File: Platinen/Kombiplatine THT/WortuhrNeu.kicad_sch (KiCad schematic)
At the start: 101 parts, among them J1 Conn_01x01_Pin, J2 PROG MODE, J3 UART FLOATING, J4 UART, J5 Eingangsbuchse, SW1 PTS645Vx83-2LFS, SW2 PTS645Vx83-2LFS, U2 MCP1826-ADJE/ET, U3 Bluepill, U4 DS18B20, U6 Arduino_Nano_Every, U7 ESP-07, U8 Generic DCDC, U9 TP582, X1 Conn_01x03_Pin, X10 Conn_01x03_Pin, X11 Conn_01x03_Pin, X12 Conn_01x03_Pin, X13 Conn_01x03_Pin, X14 Conn_01x03_Pin, X15 Conn_01x03_Pin, X16 Conn_01x03_Pin, X17 Conn_01x03_Pin, X18 Conn_01x03_Pin, X19 Conn_01x03_Pin, X2 Conn_01x03_Pin, X20 Conn_01x03_Pin, X21 Conn_01x03_Pin, X22 Conn_01x03_Pin, X23 Conn_01x03_Pin, X24 Conn_01x03_Pin, X25 Conn_01x03_Pin, X26 Conn_01x03_Pin, X27 Conn_01x03_Pin, X28 Conn_01x03_Pin, X29 Conn_01x03_Pin, X3 Conn_01x03_Pin, X30 Conn_01x03_Pin, X31 Conn_01x03_Pin, X32 Conn_01x03_Pin, X33 Conn_01x03_Pin, X34 Conn_01x03_Pin, X35 Conn_01x03_Pin, X36 Conn_01x03_Pin, X37 Conn_01x03_Pin, X38 Conn_01x03_Pin, X4 Conn_01x03_Pin, X5 Conn_01x03_Pin, X6 Conn_01x03_Pin, X7 Conn_01x03_Pin, X8 Conn_01x03_Pin, X9 Conn_01x03_Pin

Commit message: Changes to Kombiplatine THT
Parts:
- J1: footprint TestPoint:TestPoint_Pad_1.0x1.0mm -> Connector_PinHeader_2.54mm:PinHeader_1x01_P2.54mm_Vertical
- U5: value ~ -> (none)
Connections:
- net +5V: now also X10.3 (Pin_3), X11.3 (Pin_3), X12.3 (Pin_3), X13.1 (Pin_1), X14.3 (Pin_3), X15.1 (Pin_1), X16.1 (Pin_1), X17.1 (Pin_1), X18.3 (Pin_3), X6.1 (Pin_1), X7.3 (Pin_3), X8.1 (Pin_1), X9.1 (Pin_1); no longer X10.1 (Pin_1), X11.1 (Pin_1), X12.1 (Pin_1), X13.3 (Pin_3), X14.1 (Pin_1), X15.3 (Pin_3), X16.3 (Pin_3), X17.3 (Pin_3), X18.1 (Pin_1), X6.3 (Pin_3), X7.1 (Pin_1), X8.3 (Pin_3), X9.3 (Pin_3)
- net GND: now also X10.1 (Pin_1), X11.1 (Pin_1), X12.1 (Pin_1), X13.3 (Pin_3), X14.1 (Pin_1), X15.3 (Pin_3), X16.3 (Pin_3), X17.3 (Pin_3), X18.1 (Pin_1), X6.3 (Pin_3), X7.1 (Pin_1), X8.3 (Pin_3), X9.3 (Pin_3); no longer X10.3 (Pin_3), X11.3 (Pin_3), X12.3 (Pin_3), X13.1 (Pin_1), X14.3 (Pin_3), X15.1 (Pin_1), X16.1 (Pin_1), X17.1 (Pin_1), X18.3 (Pin_3), X6.1 (Pin_1), X7.3 (Pin_3), X8.1 (Pin_1), X9.1 (Pin_1)
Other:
- note added: "12-24V"

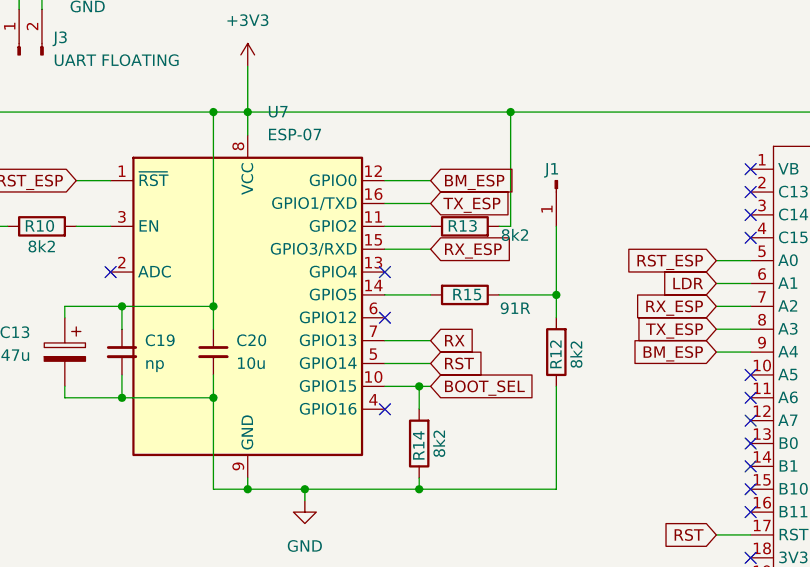
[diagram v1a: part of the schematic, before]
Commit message: Switched gpio4&5 on the esp for both boards
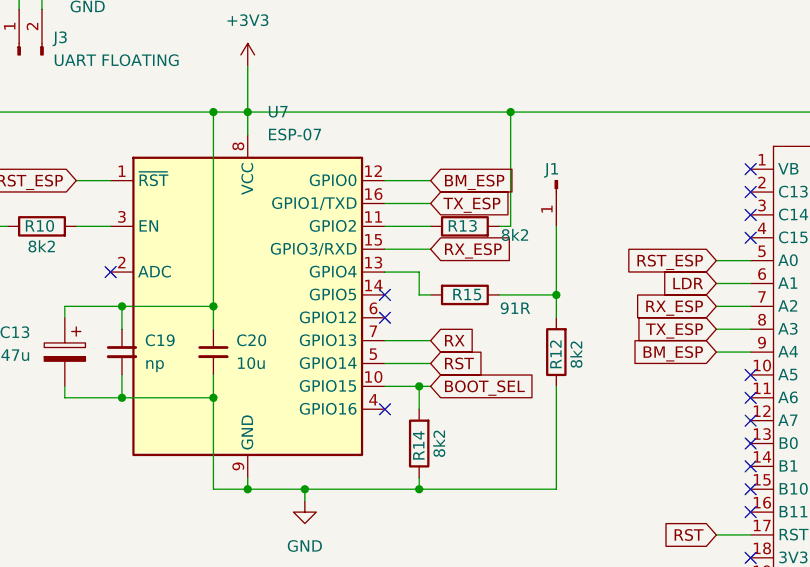
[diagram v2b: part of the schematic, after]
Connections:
- net at R15.2: now also U7.13 (GPIO4); no longer U7.14 (GPIO5)
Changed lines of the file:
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@@
 	)
 	(no_connect
+		(at 134.62 107.95)
+	)
+	(no_connect
 		(at 208.28 101.6)
 	)
@@
 	)
 	(no_connect
-		(at 134.62 105.41)
-	)
-	(no_connect
 		(at 247.65 132.08)
 	)
@@
 	(wire
 		(pts
-			(xy 134.62 107.95) (xy 139.7 107.95)
-		)
-		(stroke
-			(width 0)
-			(type default)
-		)
-	)
-	(wire
-		(pts
 			(xy 262.89 320.04) (xy 276.86 320.04)
 		)
@@
 	(wire
 		(pts
+			(xy 138.43 107.95) (xy 139.7 107.95)
+		)
+		(stroke
+			(width 0)
+			(type default)
+		)
+	)
+	(wire
+		(pts
 			(xy 265.43 77.47) (xy 265.43 87.63)
 		)
@@
 	(wire
 		(pts
+			(xy 138.43 105.41) (xy 138.43 107.95)
+		)
+		(stroke
+			(width 0)
+			(type default)
+		)
+	)
+	(wire
+		(pts
 			(xy 251.46 77.47) (xy 236.22 77.47)
 		)
@@
 		)
 		(stroke
+			(width 0)
+			(type default)
+		)
+	)
+	(wire
+		(pts
+			(xy 134.62 105.41) (xy 138.43 105.41)
+		)
+		(stroke
